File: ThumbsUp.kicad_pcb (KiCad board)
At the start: 2 copper layers, 211.3 x 236.6 mm, 62 parts, among them J1 52559-1233, J1L1 PJ-3200B, J1R1 PJ-3200B, J2 52559-1233, U1 ProMicro

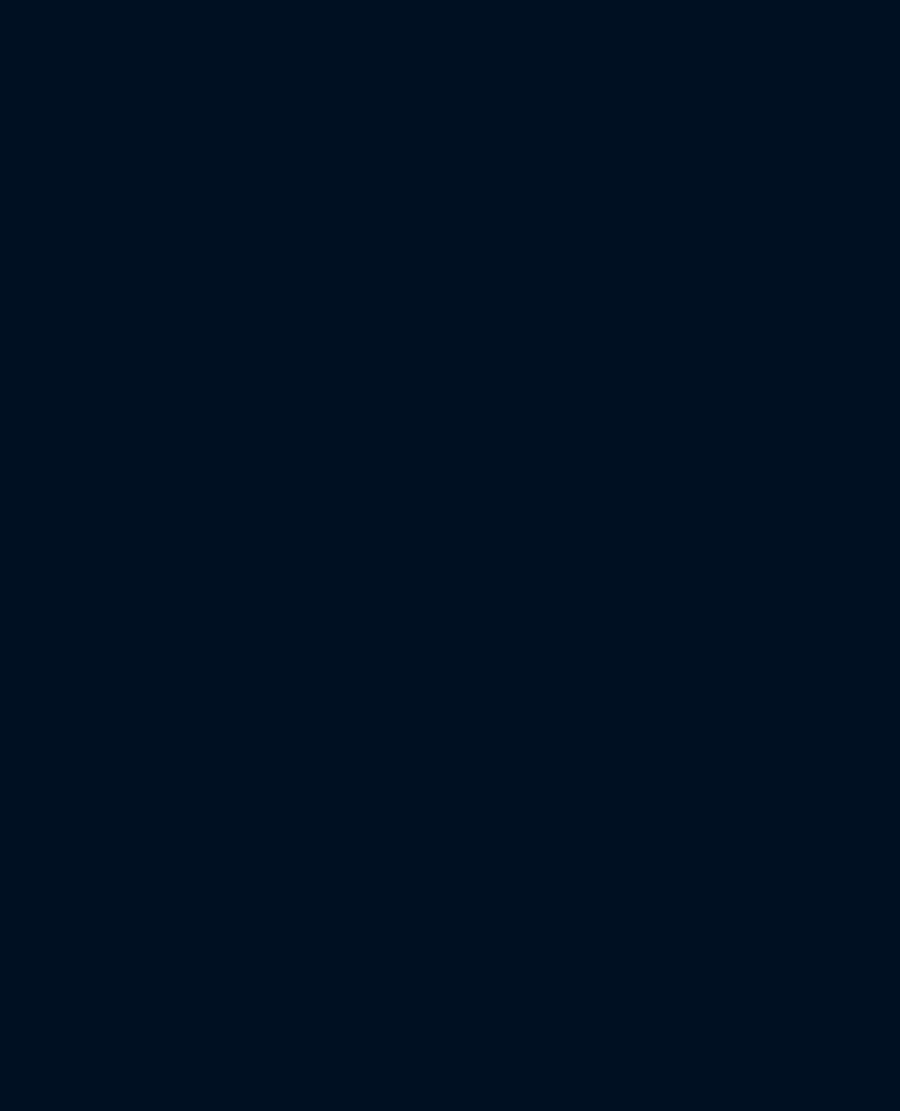
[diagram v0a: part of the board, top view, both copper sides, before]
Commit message: K12: Added overlapping key flaps, as ordered 20261022.
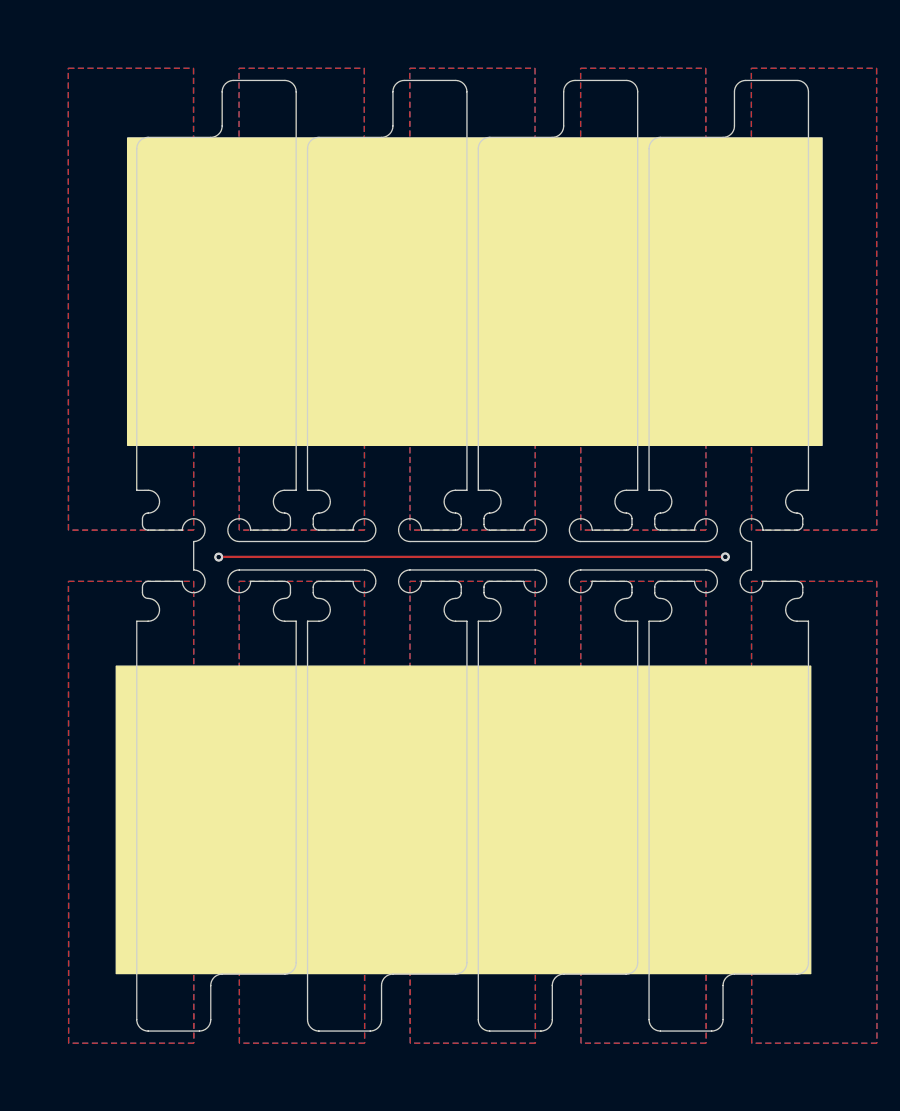
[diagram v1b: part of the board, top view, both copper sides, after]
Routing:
- net (no net): track 44.5 -> 89.0 mm, vias 2 -> 4
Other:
- board size 211.3 x 236.6 mm -> 285.3 x 236.6 mm
